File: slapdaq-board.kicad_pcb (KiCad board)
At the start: 4 copper layers, 88 x 136 mm, 74 parts, among them J1 Higher Screw Terminals, J2 Lower Screw Terminals, J3 USB-C, Q1 BSS84, U1 LM2675M-3.3, U2 LM2675M-5, U3 ESP32-S3, U4 DT1042-04SO-7, U5 REF3333, U6 ADS1261, U7 MAX31856

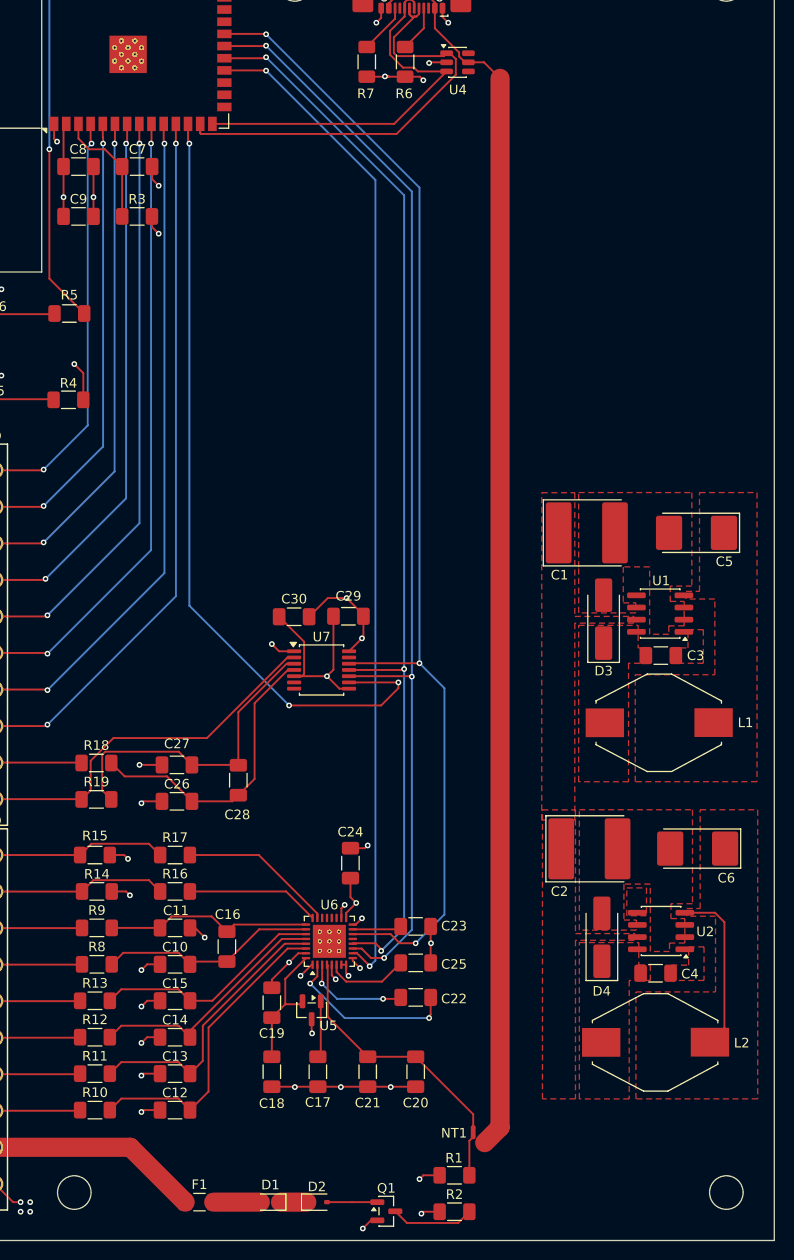
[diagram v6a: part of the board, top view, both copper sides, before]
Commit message: made traces bigger and had to move mounting hole a little down to accomodate that
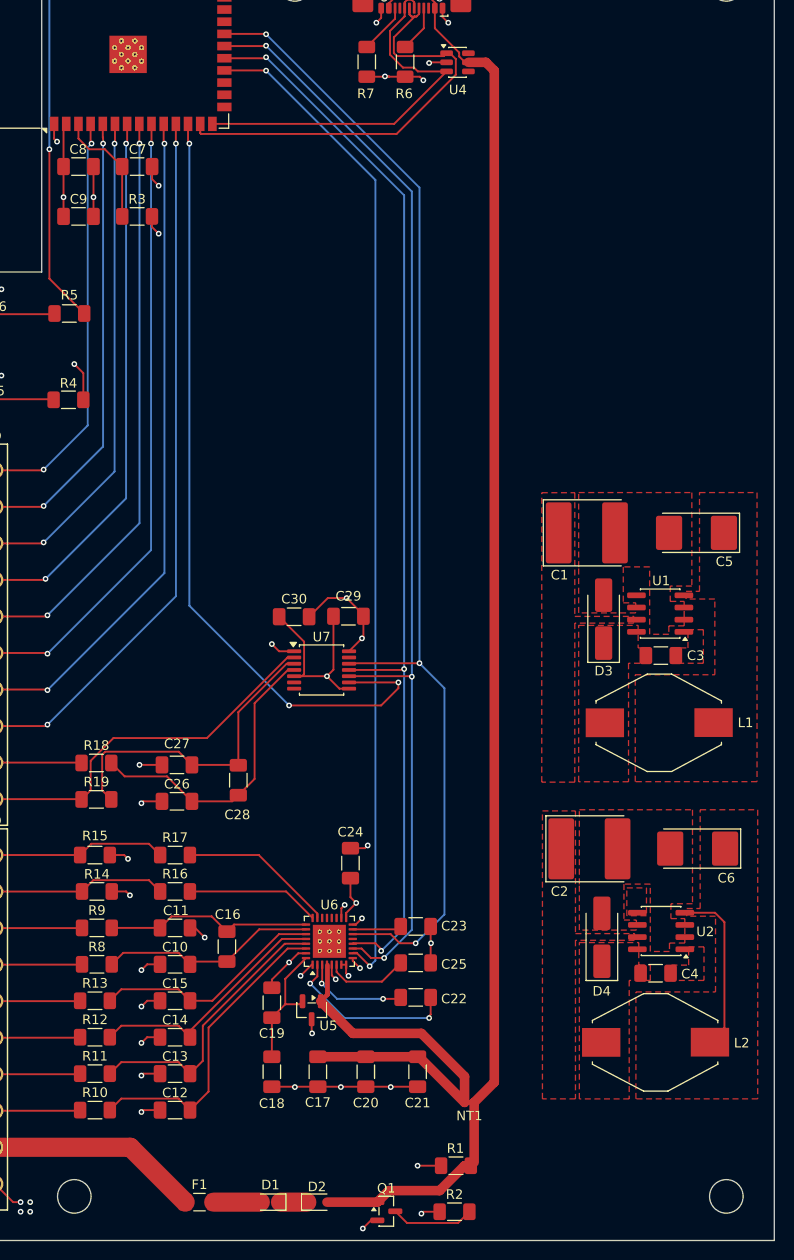
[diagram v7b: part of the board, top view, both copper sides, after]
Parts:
- moved C21 5.20 mm to (145.8, 174.4)
- moved C20 5.20 mm to (140.4, 174.4)
- moved NT1 3.13 mm to (151.2, 177.6), turned to 0 degrees
- moved R1 1.01 mm to (149.8, 184.2)
- moved REF** 0.40 mm to (110.0, 187.4)
- moved REF** 0.40 mm to (178.0, 187.4)
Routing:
- net +5V: track 49.8 -> 60.5 mm
- net Vbus: track 138.9 -> 148.6 mm
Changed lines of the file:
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@@
 	(footprint "Capacitor_SMD:C_1206_3216Metric_Pad1.33x1.80mm_HandSolder"
 		(layer "F.Cu")
-		(at 145.6 174.4 90)
+		(at 140.4 174.4 90)
 		(descr "Capacitor SMD 1206 (3216 Metric), square (rectangular) end terminal, IPC-7351 nominal with elongated pad for handsoldering. (Body size source: IPC-SM-782 page 76, https://www.pcb-3d.com/wordpress/wp-content/uploads/ipc-sm-782a_amendment_1_and_2.pdf)")
 		(tags "capacitor handsolder")
@@
 	(footprint "NetTie:NetTie-2_SMD_Pad0.5mm"
 		(layer "F.Cu")
-		(at 151.6 180.7 -90)
+		(at 151.2 177.6)
 		(descr "Net tie, 2 pin, 0.5mm square SMD pads")
 		(tags "net tie")
 		(property "Reference" "NT1"
-			(at 0.1 2 0)
+			(at 0 1.4 180)
 			(layer "F.SilkS")
 			(effects
@@
 		)
 		(property "Value" "NetTie_2"
-			(at 0 1.2 90)
+			(at 0 1.2 0)
 			(layer "F.Fab")
 			(hide yes)
@@
 		)
 		(property "Datasheet" ""
-			(at 0 0 270)
+			(at 0 0 0)
 			(unlocked yes)
 			(layer "F.Fab")
@@
 		)
 		(property "Description" "Net tie, 2 pins"
-			(at 0 0 270)
+			(at 0 0 0)
 			(unlocked yes)
 			(layer "F.Fab")
@@
 		)
 		(pad "1" smd circle
-			(at -0.5 0 270)
+			(at -0.5 0)
 			(size 0.5 0.5)
 			(layers "F.Cu")
@@
 		)
 		(pad "2" smd circle
-			(at 0.5 0 270)
+			(at 0.5 0)
 			(size 0.5 0.5)
 			(layers "F.Cu")
@@
 	(footprint "Capacitor_SMD:C_1206_3216Metric_Pad1.33x1.80mm_HandSolder"
 		(layer "F.Cu")
-		(at 140.6 174.4 90)
+		(at 145.8 174.4 90)
 		(descr "Capacitor SMD 1206 (3216 Metric), square (rectangular) end terminal, IPC-7351 nominal with elongated pad for handsoldering. (Body size source: IPC-SM-782 page 76, https://www.pcb-3d.com/wordpress/wp-content/uploads/ipc-sm-782a_amendment_1_and_2.pdf)")
 		(tags "capacitor handsolder")
@@
 	(footprint "MountingHole:MountingHole_3.5mm"
 		(layer "F.Cu")
-		(at 110 187)
+		(at 110 187.4)
 		(descr "Mounting Hole 3.5mm, no annular, generated by kicad-footprint-generator mountinghole.py")
 		(tags "mountinghole")
@@
 	(footprint "Resistor_SMD:R_1206_3216Metric_Pad1.30x1.75mm_HandSolder"
 		(layer "F.Cu")
-		(at 149.65 185.2 180)
+		(at 149.8 184.2 180)
 		(descr "Resistor SMD 1206 (3216 Metric), square (rectangular) end terminal, IPC-7351 nominal with elongated pad for handsoldering. (Body size source: IPC-SM-782 page 72, https://www.pcb-3d.com/wordpress/wp-content/uploads/ipc-sm-782a_amendment_1_and_2.pdf)")
 		(tags "resistor handsolder")
@@
 	(footprint "MountingHole:MountingHole_3.5mm"
 		(layer "F.Cu")
-		(at 178 187)
+		(at 178 187.4)
 		(descr "Mounting Hole 3.5mm, no annular, generated by kicad-footprint-generator mountinghole.py")
 		(tags "mountinghole")
@@
 	)
 	(segment
+		(start 151.35 184.2)
+		(end 150.7 184.2)
+		(width 1)
+		(layer "F.Cu")
+		(net "Vbus")
+	)
+	(segment
 		(start 136.35 188)
-		(end 139 188)
-		(width 0.2)
+		(end 141.6 188)
+		(width 1)
 		(layer "F.Cu")
 		(net "Vbus")
 	)
 	(segment
-		(start 142.8 62.98)
-		(end 143.575 62.205)
-		(width 0.2)
+		(start 148.1 186.8)
+		(end 142.8 186.8)
+		(width 1)
 		(layer "F.Cu")
 		(net "Vbus")
 	)
 	(segment
-		(start 151.2 185.2)
-		(end 151.2 181.6)
+		(start 142.8 62.98)
+		(end 143.575 62.205)
 		(width 0.2)
 		(layer "F.Cu")
@@
 	)
 	(segment
-		(start 154.4 180.2)
-		(end 152.8 181.8)
-		(width 2)
+		(start 151.35 184.2)
+		(end 151.7 183.85)
+		(width 0.2)
 		(layer "F.Cu")
 		(net "Vbus")
@@
 	)
 	(segment
-		(start 141.6 188)
-		(end 139 188)
-		(width 0.2)
+		(start 153.8 175.5)
+		(end 151.7 177.6)
+		(width 1)
+		(layer "F.Cu")
+		(net "Vbus")
+	)
+	(segment
+		(start 151.1 69.13)
+		(end 152.93 69.13)
+		(width 1)
 		(layer "F.Cu")
 		(net "Vbus")
@@
 	)
 	(segment
-		(start 151.2 181.6)
-		(end 151.6 181.2)
-		(width 0.2)
+		(start 150.7 184.2)
+		(end 148.1 186.8)
+		(width 1)
 		(layer "F.Cu")
 		(net "Vbus")
@@
 	)
 	(segment
-		(start 154.4 70.8)
-		(end 152.73 69.13)
-		(width 0.2)
-		(layer "F.Cu")
-		(net "Vbus")
-	)
-	(segment
-		(start 152.73 69.13)
-		(end 151.1 69.13)
-		(width 0.2)
+		(start 153.8 70)
+		(end 153.8 175.5)
+		(width 1)
 		(layer "F.Cu")
 		(net "Vbus")
@@
 	)
 	(segment
-		(start 154.4 70.8)
-		(end 154.4 180.2)
-		(width 2)
+		(start 151.7 183.85)
+		(end 151.7 177.6)
+		(width 1)
+		(layer "F.Cu")
+		(net "Vbus")
+	)
+	(segment
+		(start 152.93 69.13)
+		(end 153.8 70)
+		(width 1)
+		(layer "F.Cu")
+		(net "Vbus")
+	)
+	(segment
+		(start 142.8 186.8)
+		(end 141.6 188)
+		(width 1)
 		(layer "F.Cu")
 		(net "Vbus")
@@
 	)
 	(segment
-		(start 148.1 185.2)
-		(end 146.4 185.2)
+		(start 107.89 77.09)
+		(end 108.2 77.4)
 		(width 0.2)
 		(layer "F.Cu")
@@
 	)
 	(segment
-		(start 107.89 77.09)
-		(end 108.2 77.4)
+		(start 148.25 184.2)
+		(end 145.8 184.2)
 		(width 0.2)
 		(layer "F.Cu")
@@
 	)
 	(segment
-		(start 146.4 185.2)
-		(end 146 185.6)
-		(width 0.2)
-		(layer "F.Cu")
-		(net "GND")
-	)
-	(segment
 		(start 150.31 61)
 		(end 150.31 62.905)
@@
 	)
 	(via
-		(at 146 185.6)
+		(at 145.8 184.2)
 		(size 0.6)
 		(drill 0.3)
@@
 	)
 	(segment
-		(start 151.6 178.8375)
-		(end 151.6 180.2)
-		(width 0.2)
+		(start 150.7 174.9)
+		(end 150.7 177.6)
+		(width 1)
 		(layer "F.Cu")
 		(net "+5V")
 	)
 	(segment
-		(start 177.8 169.809314)
-		(end 176.29 171.319314)
-		(width 0.2)
+		(start 146.2 170.4)
+		(end 150.7 174.9)
+		(width 1)
 		(layer "F.Cu")
 		(net "+5V")
 	)
 	(segment
-		(start 145.6 172.8375)
-		(end 151.6 178.8375)
-		(width 0.2)
+		(start 150.7 177.6)
+		(end 145.9375 172.8375)
+		(width 1)
 		(layer "F.Cu")
 		(net "+5V")
 	)
 	(segment
-		(start 135.7 172.5375)
-		(end 135.4 172.8375)
-		(width 0.2)
+		(start 136.4 163.2875)
+		(end 136.4 166.35)
+		(width 0.5)
 		(layer "F.Cu")
 		(net "+5V")
 	)
 	(segment
-		(start 140.6 172.8375)
-		(end 136.425 168.6625)
+		(start 177.8 169.809314)
+		(end 176.29 171.319314)
 		(width 0.2)
 		(layer "F.Cu")
@@
 	)
 	(segment
-		(start 136.425 163.3125)
-		(end 136.35 163.2375)
-		(width 0.2)
+		(start 139.05 170.4)
+		(end 146.2 170.4)
+		(width 1)
 		(layer "F.Cu")
 		(net "+5V")
 	)
 	(segment
-		(start 135.7 167.05)
-		(end 135.7 172.5375)
+		(start 135.7 172.5375)
+		(end 135.4 172.8375)
 		(width 0.2)
 		(layer "F.Cu")
@@
 	)
 	(segment
-		(start 136.425 168.6625)
-		(end 136.425 163.3125)
-		(width 0.2)
+		(start 145.9375 172.8375)
+		(end 135.4 172.8375)
+		(width 1)
 		(layer "F.Cu")
 		(net "+5V")
 	)
 	(segment
-		(start 140.6 172.8375)
-		(end 145.6 172.8375)
+		(start 136.35 163.2375)
+		(end 136.4 163.2875)
 		(width 0.2)
 		(layer "F.Cu")
@@
 	)
 	(segment
+		(start 136.4 166.35)
+		(end 135.7 167.05)
+		(width 0.5)
+		(layer "F.Cu")
+		(net "+5V")
+	)
+	(segment
 		(start 177.8 158.8)
 		(end 177.8 169.809314)
@@
 	)
 	(segment
+		(start 135.7 167.05)
+		(end 139.05 170.4)
+		(width 1)
+		(layer "F.Cu")
+		(net "+5V")
+	)
+	(segment
 		(start 147.1625 168.4375)
 		(end 147.1625 166.65)
@@
 		(polygon
 			(pts
-				(xy 158.82 177.229314) (xy 158.82 147.093834) (xy 162.264715 147.093834) (xy 162.264715 159.993834)
-				(xy 168.42 159.993834) (xy 168.42 160.693834) (xy 162.264715 160.693834) (xy 162.264715 177.229314)
+				(xy 158.82 177.229314) (xy 158.82 147.2) (xy 162.264715 147.2) (xy 162.264715 159.993834) (xy 168.42 159.993834)
+				(xy 168.42 160.693834) (xy 162.264715 160.693834) (xy 162.264715 177.229314)
 			)
 		)
@@
 		(polygon
 			(pts
-				(xy 158.75 148.15) (xy 158.75 114.01452) (xy 162.194715 114.01452) (xy 162.194715 126.91452) (xy 168.35 126.91452)
-				(xy 168.35 127.61452) (xy 162.194715 127.61452) (xy 162.194715 148.15)
+				(xy 158.75 144.2) (xy 158.75 114.01452) (xy 162.194715 114.01452) (xy 162.194715 126.91452) (xy 168.35 126.91452)
+				(xy 168.35 127.61452) (xy 162.194715 127.61452) (xy 162.194715 144.2)
 			)
 		)

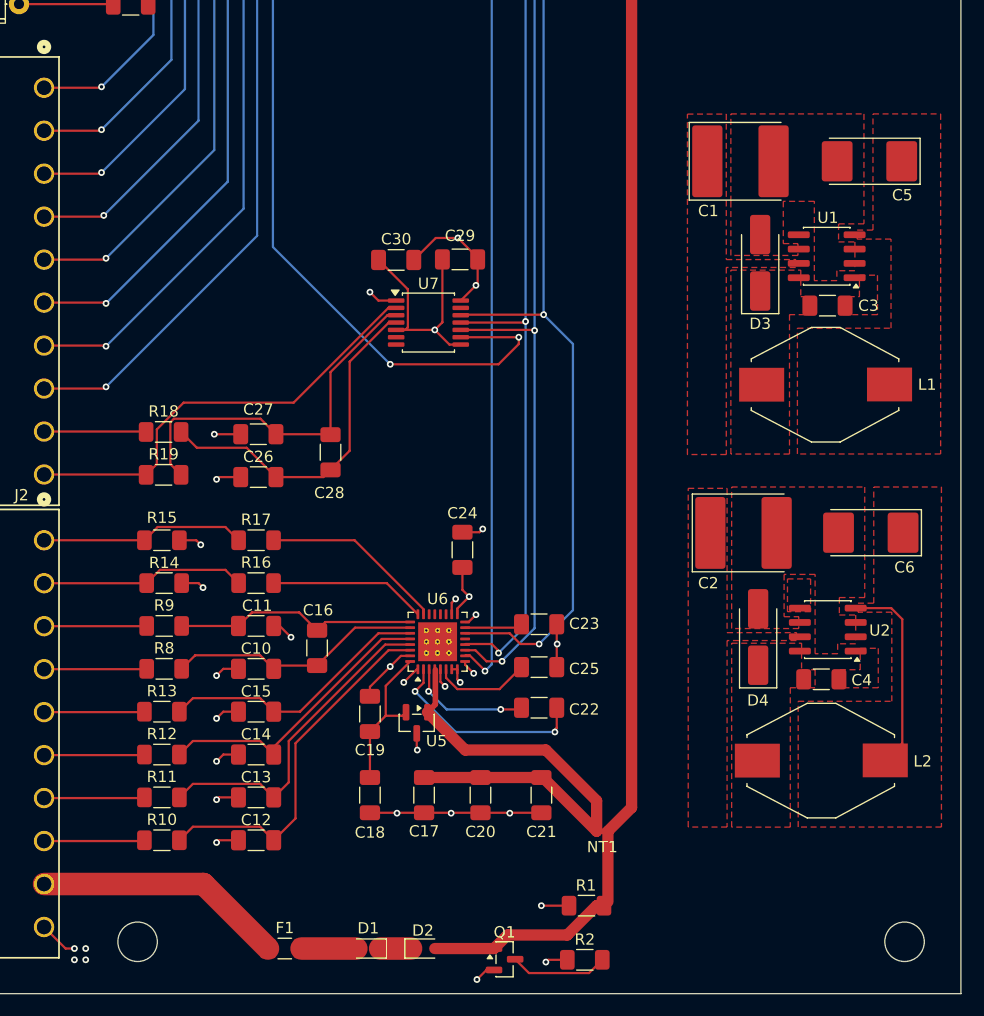
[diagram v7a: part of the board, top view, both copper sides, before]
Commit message: added zone around ground vias and added vias for 3.3V
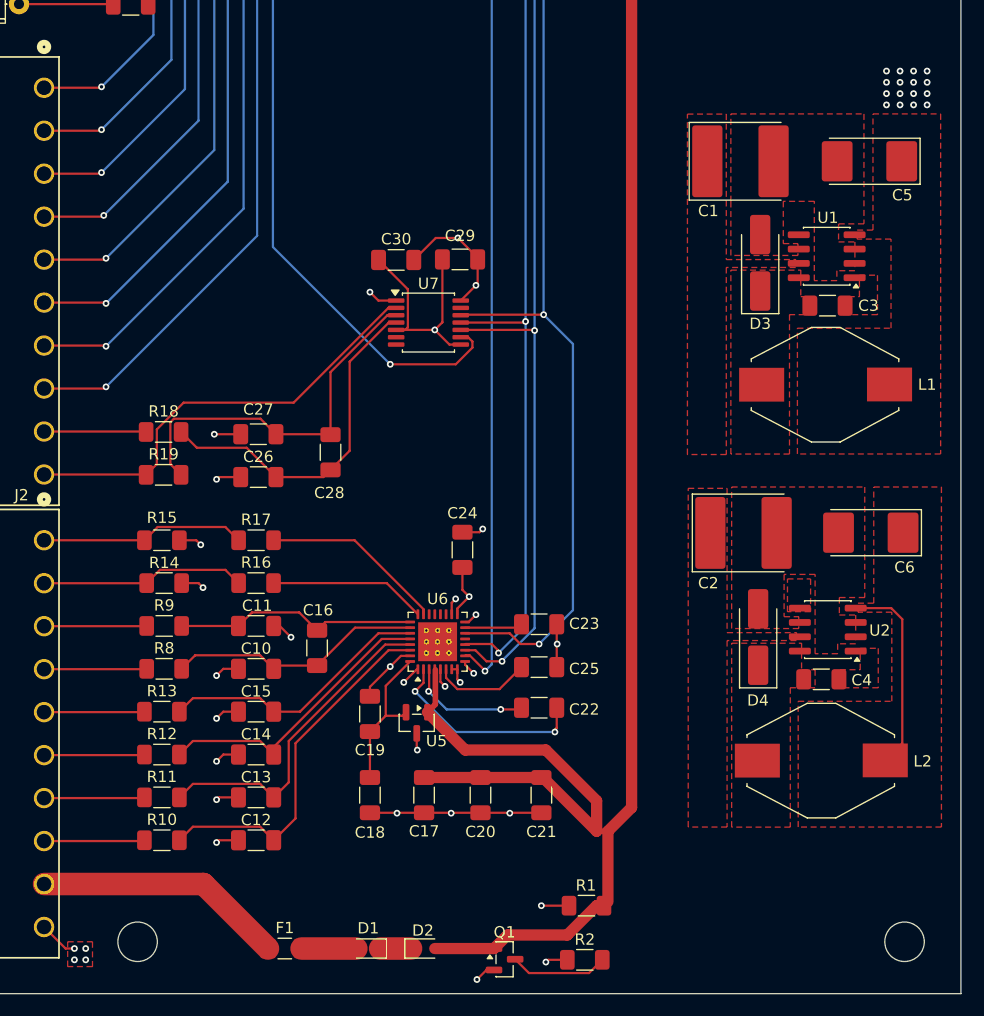
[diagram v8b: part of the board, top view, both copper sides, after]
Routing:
- net CS1_THR: track 82.9 -> 74.6 mm, vias 3 -> 2
- net +3.3V: vias 7 -> 23
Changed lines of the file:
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@@
 			(at 0 1.4 180)
 			(layer "F.SilkS")
+			(hide yes)
 			(effects
 				(font
@@
 	)
 	(via
+		(at 180 113.2)
+		(size 0.6)
+		(drill 0.3)
+		(layers "F.Cu" "B.Cu")
+		(free yes)
+		(net "+3.3V")
+	)
+	(via
+		(at 176.4 113.2)
+		(size 0.6)
+		(drill 0.3)
+		(layers "F.Cu" "B.Cu")
+		(free yes)
+		(net "+3.3V")
+	)
+	(via
+		(at 178.8 110.2)
+		(size 0.6)
+		(drill 0.3)
+		(layers "F.Cu" "B.Cu")
+		(free yes)
+		(net "+3.3V")
+	)
+	(via
+		(at 180 111.2)
+		(size 0.6)
+		(drill 0.3)
+		(layers "F.Cu" "B.Cu")
+		(free yes)
+		(net "+3.3V")
+	)
+	(via
+		(at 180 110.2)
+		(size 0.6)
+		(drill 0.3)
+		(layers "F.Cu" "B.Cu")
+		(free yes)
+		(net "+3.3V")
+	)
+	(via
 		(at 138.6 164.4)
 		(size 0.6)
@@
 	)
 	(via
+		(at 178.8 112.2)
+		(size 0.6)
+		(drill 0.3)
+		(layers "F.Cu" "B.Cu")
+		(free yes)
+		(net "+3.3V")
+	)
+	(via
+		(at 178.8 111.2)
+		(size 0.6)
+		(drill 0.3)
+		(layers "F.Cu" "B.Cu")
+		(free yes)
+		(net "+3.3V")
+	)
+	(via
 		(at 140.0875 190.75)
 		(size 0.6)
@@
 	)
 	(via
+		(at 176.4 112.2)
+		(size 0.6)
+		(drill 0.3)
+		(layers "F.Cu" "B.Cu")
+		(free yes)
+		(net "+3.3V")
+	)
+	(via
+		(at 177.6 110.2)
+		(size 0.6)
+		(drill 0.3)
+		(layers "F.Cu" "B.Cu")
+		(free yes)
+		(net "+3.3V")
+	)
+	(via
+		(at 176.4 111.2)
+		(size 0.6)
+		(drill 0.3)
+		(layers "F.Cu" "B.Cu")
+		(free yes)
+		(net "+3.3V")
+	)
+	(via
+		(at 178.8 113.2)
+		(size 0.6)
+		(drill 0.3)
+		(layers "F.Cu" "B.Cu")
+		(free yes)
+		(net "+3.3V")
+	)
+	(via
+		(at 177.6 112.2)
+		(size 0.6)
+		(drill 0.3)
+		(layers "F.Cu" "B.Cu")
+		(free yes)
+		(net "+3.3V")
+	)
+	(via
 		(at 108.875 83.2)
 		(size 0.6)
@@
 	)
 	(via
+		(at 180 112.2)
+		(size 0.6)
+		(drill 0.3)
+		(layers "F.Cu" "B.Cu")
+		(free yes)
+		(net "+3.3V")
+	)
+	(via
 		(at 110 100.6)
 		(size 0.6)
@@
 	)
 	(via
+		(at 177.6 111.2)
+		(size 0.6)
+		(drill 0.3)
+		(layers "F.Cu" "B.Cu")
+		(free yes)
+		(net "+3.3V")
+	)
+	(via
+		(at 177.6 113.2)
+		(size 0.6)
+		(drill 0.3)
+		(layers "F.Cu" "B.Cu")
+		(free yes)
+		(net "+3.3V")
+	)
+	(via
+		(at 176.4 110.2)
+		(size 0.6)
+		(drill 0.3)
+		(layers "F.Cu" "B.Cu")
+		(free yes)
+		(net "+3.3V")
+	)
+	(via
 		(at 139.4 156.8)
 		(size 0.6)
@@
 	)
 	(segment
-		(start 142 136.2)
-		(end 143.8 134.4)
+		(start 139.6875 134.181544)
+		(end 139.6875 134.718456)
 		(width 0.2)
 		(layer "F.Cu")
@@
 	)
 	(segment
-		(start 143.8 133.8)
-		(end 138.65 133.8)
+		(start 139.6875 134.718456)
+		(end 138.205956 136.2)
 		(width 0.2)
 		(layer "F.Cu")
@@
 	)
 	(segment
-		(start 143.8 134.4)
-		(end 143.8 133.8)
+		(start 138.65 133.8)
+		(end 139.305956 133.8)
 		(width 0.2)
 		(layer "F.Cu")
@@
 	)
 	(segment
-		(start 132.4 136.2)
-		(end 142 136.2)
+		(start 121.86 75.55)
+		(end 121.86 77.46)
 		(width 0.2)
 		(layer "F.Cu")
@@
 	)
 	(segment
-		(start 121.86 75.55)
-		(end 121.86 77.46)
+		(start 139.305956 133.8)
+		(end 139.6875 134.181544)
 		(width 0.2)
 		(layer "F.Cu")
@@
 		(net "CS1_THR")
 	)
-	(via
-		(at 132.4 136.2)
-		(size 0.6)
-		(drill 0.3)
-		(layers "F.Cu" "B.Cu")
+	(segment
+		(start 138.205956 136.2)
+		(end 132.4 136.2)
+		(width 0.2)
+		(layer "F.Cu")
 		(net "CS1_THR")
 	)
 	(via
-		(at 122 77.6)
+		(at 132.4 136.2)
 		(size 0.6)
 		(drill 0.3)
@@
 	)
 	(via
-		(at 143.8 133.8)
+		(at 122 77.6)
 		(size 0.6)
 		(drill 0.3)
@@
 			)
 		)
+	)
+	(zone
+		(net "GND")
+		(layer "F.Cu")
+		(hatch edge 0.5)
+		(priority 7)
+		(connect_pads yes
+			(clearance 0.2)
+		)
+		(min_thickness 0.25)
+		(fill
+			(thermal_gap 0.5)
+			(thermal_bridge_width 0.5)
+			(island_removal_mode 0)
+		)
+		(polygon
+			(pts
+				(xy 103.8 187.4) (xy 106 187.4) (xy 106 189.6) (xy 103.8 189.6)
+			)
+		)
